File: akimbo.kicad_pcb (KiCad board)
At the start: 2 copper layers, 163.9 x 125.9 mm, 73 parts, among them J1 USB mini-B, J2 3.5mm TRRS, J3 3.5mm TRRS, K1 -, K11 -, K12 -, K13 -, K14 -, K15 -, K16 -, K17 -, K18 -, K19 -, K2 -, K20 -, K21 -, K22 -, K23 -, K24 -, K25 -, K26 -, K27 -, K28 -, K29 -, K3 -, K30 -, K4 -, K6 -, K7 -, K8 -, K9 -, U1 ATmega32U4, U2 MCP23017_SO, Y1 16M

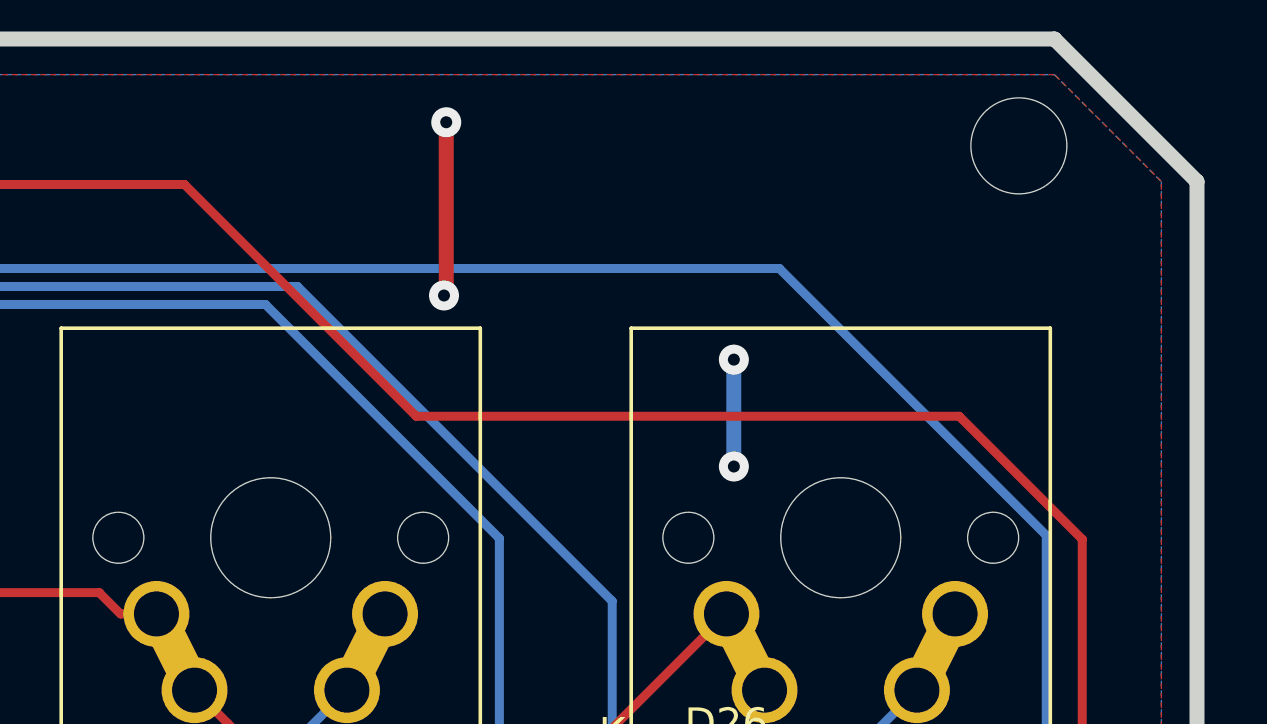
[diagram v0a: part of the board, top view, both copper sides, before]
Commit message: I2C pullups
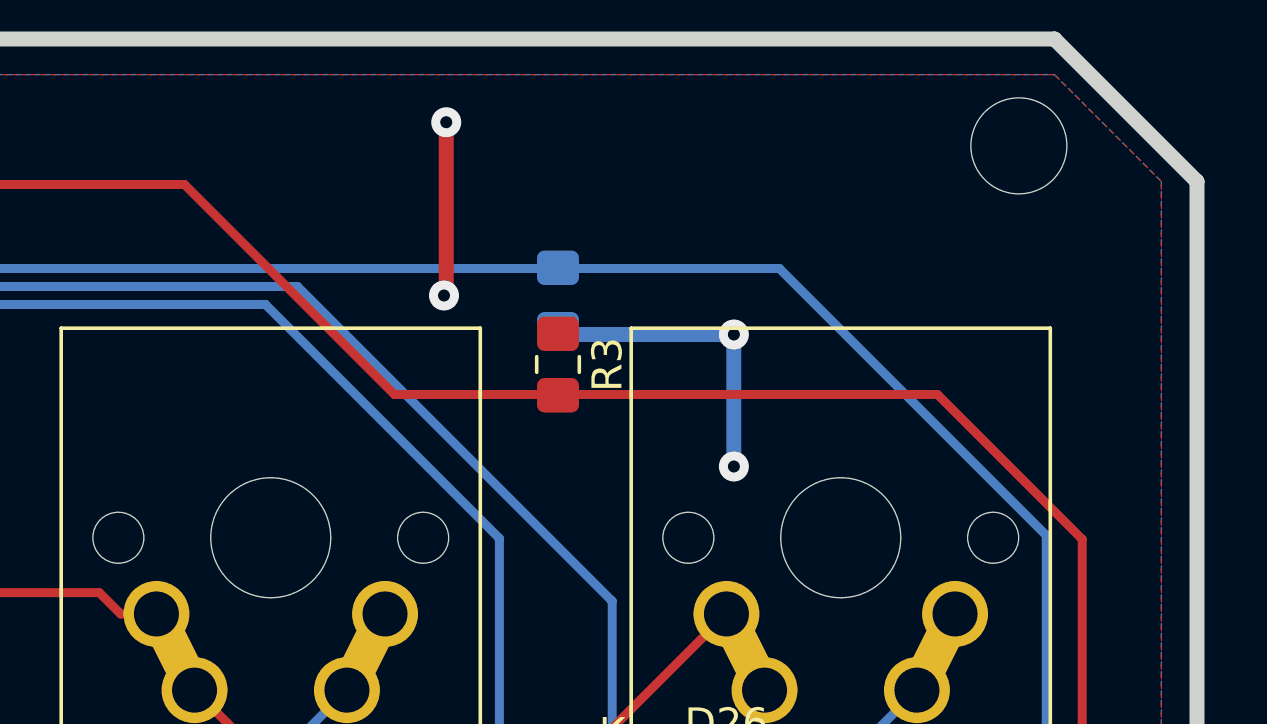
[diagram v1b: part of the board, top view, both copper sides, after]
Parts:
- added R3: 4k7, Resistor_SMD:R_0805_2012Metric_Pad1.15x1.40mm_HandSolder, F.Cu at (121.2, 34.6)
- added R4: 4k7, Resistor_SMD:R_0805_2012Metric_Pad1.15x1.40mm_HandSolder, B.Cu at (121.2, 32.4)
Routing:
- net +5V: track 66.8 -> 73.6 mm
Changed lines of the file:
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@@
     (thickness 1.6)
     (drawings 17)
-    (tracks 577)
+    (tracks 581)
     (zones 0)
-    (modules 73)
+    (modules 75)
     (nets 51)
   )
@@
     (add_net GND)
   )
+  (module Resistor_SMD:R_0805_2012Metric_Pad1.15x1.40mm_HandSolder (layer B.Cu)
+    (at 121.2 32.4 90)
+    (descr "Resistor SMD 0805 (2012 Metric), square (rectangular) end terminal, IPC_7351 nominal with elongated pad for handsoldering. (Body size source: https://docs.google.com/spreadsheets/d/1BsfQQcO9C6DZCsRaXUlFlo91Tg2WpOkGARC1WS5S8t0/edit?usp=sharing), generated with kicad-footprint-generator")
+    (tags "resistor handsolder")
+    (attr smd)
+    (fp_text reference R4 (at 0 1.65 270) (layer B.SilkS)
+      (effects (font (size 1 1) (thickness 0.15)) (justify mirror))
+    )
+    (fp_text value 4k7 (at 0 -1.65 270) (layer B.Fab)
+      (effects (font (size 1 1) (thickness 0.15)) (justify mirror))
+    )
+    (fp_text user %R (at 0 0 270) (layer B.Fab)
+      (effects (font (size 0.5 0.5) (thickness 0.08)) (justify mirror))
+    )
+    (fp_line (start 1.85 -0.95) (end -1.85 -0.95) (layer B.CrtYd) (width 0.05))
+    (fp_line (start 1.85 0.95) (end 1.85 -0.95) (layer B.CrtYd) (width 0.05))
+    (fp_line (start -1.85 0.95) (end 1.85 0.95) (layer B.CrtYd) (width 0.05))
+    (fp_line (start -1.85 -0.95) (end -1.85 0.95) (layer B.CrtYd) (width 0.05))
+    (fp_line (start -0.261252 -0.71) (end 0.261252 -0.71) (layer B.SilkS) (width 0.12))
+    (fp_line (start -0.261252 0.71) (end 0.261252 0.71) (layer B.SilkS) (width 0.12))
+    (fp_line (start 1 -0.6) (end -1 -0.6) (layer B.Fab) (width 0.1))
+    (fp_line (start 1 0.6) (end 1 -0.6) (layer B.Fab) (width 0.1))
+    (fp_line (start -1 0.6) (end 1 0.6) (layer B.Fab) (width 0.1))
+    (fp_line (start -1 -0.6) (end -1 0.6) (layer B.Fab) (width 0.1))
+    (pad 2 smd roundrect (at 1.025 0 90) (size 1.15 1.4) (layers B.Cu B.Paste B.Mask) (roundrect_rratio 0.217391)
+      (net 47 /sda))
+    (pad 1 smd roundrect (at -1.025 0 90) (size 1.15 1.4) (layers B.Cu B.Paste B.Mask) (roundrect_rratio 0.217391)
+      (net 3 +5V))
+    (model ${KISYS3DMOD}/Resistor_SMD.3dshapes/R_0805_2012Metric.wrl
+      (at (xyz 0 0 0))
+      (scale (xyz 1 1 1))
+      (rotate (xyz 0 0 0))
+    )
+  )
+  (module Resistor_SMD:R_0805_2012Metric_Pad1.15x1.40mm_HandSolder (layer F.Cu)
+    (at 121.2 34.6 270)
+    (descr "Resistor SMD 0805 (2012 Metric), square (rectangular) end terminal, IPC_7351 nominal with elongated pad for handsoldering. (Body size source: https://docs.google.com/spreadsheets/d/1BsfQQcO9C6DZCsRaXUlFlo91Tg2WpOkGARC1WS5S8t0/edit?usp=sharing), generated with kicad-footprint-generator")
+    (tags "resistor handsolder")
+    (attr smd)
+    (fp_text reference R3 (at 0 -1.65 90) (layer F.SilkS)
+      (effects (font (size 1 1) (thickness 0.15)))
+    )
+    (fp_text value 4k7 (at 0 1.65 90) (layer F.Fab)
+      (effects (font (size 1 1) (thickness 0.15)))
+    )
+    (fp_text user %R (at 0 0 90) (layer F.Fab)
+      (effects (font (size 0.5 0.5) (thickness 0.08)))
+    )
+    (fp_line (start 1.85 0.95) (end -1.85 0.95) (layer F.CrtYd) (width 0.05))
+    (fp_line (start 1.85 -0.95) (end 1.85 0.95) (layer F.CrtYd) (width 0.05))
+    (fp_line (start -1.85 -0.95) (end 1.85 -0.95) (layer F.CrtYd) (width 0.05))
+    (fp_line (start -1.85 0.95) (end -1.85 -0.95) (layer F.CrtYd) (width 0.05))
+    (fp_line (start -0.261252 0.71) (end 0.261252 0.71) (layer F.SilkS) (width 0.12))
+    (fp_line (start -0.261252 -0.71) (end 0.261252 -0.71) (layer F.SilkS) (width 0.12))
+    (fp_line (start 1 0.6) (end -1 0.6) (layer F.Fab) (width 0.1))
+    (fp_line (start 1 -0.6) (end 1 0.6) (layer F.Fab) (width 0.1))
+    (fp_line (start -1 -0.6) (end 1 -0.6) (layer F.Fab) (width 0.1))
+    (fp_line (start -1 0.6) (end -1 -0.6) (layer F.Fab) (width 0.1))
+    (pad 2 smd roundrect (at 1.025 0 270) (size 1.15 1.4) (layers F.Cu F.Paste F.Mask) (roundrect_rratio 0.217391)
+      (net 48 /sck))
+    (pad 1 smd roundrect (at -1.025 0 270) (size 1.15 1.4) (layers F.Cu F.Paste F.Mask) (roundrect_rratio 0.217391)
+      (net 3 +5V))
+    (model ${KISYS3DMOD}/Resistor_SMD.3dshapes/R_0805_2012Metric.wrl
+      (at (xyz 0 0 0))
+      (scale (xyz 1 1 1))
+      (rotate (xyz 0 0 0))
+    )
+  )
   (module akimbo:SW_Cherry_MX_1.00u_PCB_Reversible (layer F.Cu)
     (at 149.186846 109.486022 135)
@@
   (segment (start 27.675 97.125) (end 31.275 97.125) (width 0.5) (layer B.Cu) (net 3))
   (via (at 24.275 76.725) (size 1) (drill 0.4) (layers F.Cu B.Cu) (net 3))
-  (via (at 127.0625 34.4375) (size 1) (drill 0.4) (layers F.Cu B.Cu) (net 3))
   (via (at 127.0625 38) (size 1) (drill 0.4) (layers F.Cu B.Cu) (net 3))
-  (segment (start 127.0625 34.4375) (end 127.0625 38) (width 0.5) (layer B.Cu) (net 3))
   (via (at 49.8 43) (size 1) (drill 0.4) (layers F.Cu B.Cu) (net 3))
   (segment (start 51.375 39.625) (end 51.375 41.425) (width 0.5) (layer B.Cu) (net 3))
@@
   (segment (start 24.275 58.525) (end 28.4 58.525) (width 0.5) (layer B.Cu) (net 3))
   (via (at 28.4 58.525) (size 1) (drill 0.4) (layers F.Cu B.Cu) (net 3))
+  (via (at 127.062494 33.6) (size 1) (drill 0.4) (layers F.Cu B.Cu) (net 3))
+  (segment (start 127.0625 33.600006) (end 127.062494 33.6) (width 0.5) (layer B.Cu) (net 3))
+  (segment (start 127.0625 38) (end 127.0625 33.600006) (width 0.5) (layer B.Cu) (net 3))
+  (segment (start 121.225 33.6) (end 121.2 33.575) (width 0.5) (layer F.Cu) (net 3))
+  (segment (start 121.375 33.6) (end 121.2 33.425) (width 0.5) (layer B.Cu) (net 3))
+  (segment (start 127.062494 33.6) (end 121.375 33.6) (width 0.5) (layer B.Cu) (net 3))
   (segment (start 41.97 72.4375) (end 40.87 72.4375) (width 0.3) (layer B.Cu) (net 4) (status 20))
   (segment (start 43.245 71.1625) (end 41.97 72.4375) (width 0.3) (layer B.Cu) (net 4))
@@
   (segment (start 57.875 29.925) (end 57.875 32.325) (width 0.3) (layer B.Cu) (net 48))
   (segment (start 57.075 33.125) (end 56.675 33.525) (width 0.3) (layer F.Cu) (net 48))
-  (segment (start 116.475 36.325) (end 108.75 28.6) (width 0.3) (layer F.Cu) (net 48))
   (segment (start 108.75 28.6) (end 73.2 28.6) (width 0.3) (layer F.Cu) (net 48))
   (segment (start 68.675 33.125) (end 57.075 33.125) (width 0.3) (layer F.Cu) (net 48))
-  (segment (start 73.2 28.6) (end 68.675 33.125) (width 0.3) (layer F.Cu) (net 48))
-  (segment (start 134.572256 36.325) (end 116.475 36.325) (width 0.3) (layer F.Cu) (net 48))
-  (segment (start 138.675 40.427744) (end 134.572256 36.325) (width 0.3) (layer F.Cu) (net 48))
   (segment (start 138.675 83.030886) (end 138.675 40.427744) (width 0.3) (layer F.Cu) (net 48))
   (segment (start 143.722057 88.077943) (end 138.675 83.030886) (width 0.3) (layer F.Cu) (net 48))
+  (segment (start 133.847256 35.6) (end 115.75 35.6) (width 0.3) (layer F.Cu) (net 48))
+  (segment (start 73.2 28.6) (end 68.675 33.125) (width 0.3) (layer F.Cu) (net 48))
+  (segment (start 138.675 40.427744) (end 133.847256 35.6) (width 0.3) (layer F.Cu) (net 48))
+  (segment (start 115.75 35.6) (end 108.75 28.6) (width 0.3) (layer F.Cu) (net 48))
   (segment (start 72.675 27.05) (end 72.6 26.975) (width 0.3) (layer B.Cu) (net 49))
   (segment (start 77.35 27.05) (end 72.675 27.05) (width 0.3) (layer B.Cu) (net 49))
@@
     (connect_pads (clearance 0.25))
     (min_thickness 0.25)
-    (fill yes (arc_segments 32) (thermal_gap 0.25) (thermal_bridge_width 0.5))
+    (fill (arc_segments 32) (thermal_gap 0.25) (thermal_bridge_width 0.5))
     (polygon
       (pts
@@
     (connect_pads (clearance 0.25))
     (min_thickness 0.25)
-    (fill yes (arc_segments 32) (thermal_gap 0.25) (thermal_bridge_width 0.5))
+    (fill (arc_segments 32) (thermal_gap 0.25) (thermal_bridge_width 0.5))
     (polygon
       (pts
@@
     (connect_pads (clearance 0.25))
     (min_thickness 0.25)
-    (fill yes (arc_segments 32) (thermal_gap 0.25) (thermal_bridge_width 0.5))
+    (fill (arc_segments 32) (thermal_gap 0.25) (thermal_bridge_width 0.5))
     (polygon
       (pts

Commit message: Tweaked silkscreen; routing tweaks; cleanup
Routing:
- net +5V: track 73.6 -> 85.6 mm, vias 15 -> 16
- net /row3: track 224.7 -> 222.3 mm
- net /row2: track 202.6 -> 201.1 mm
- net /row1: track 178.3 -> 177.6 mm

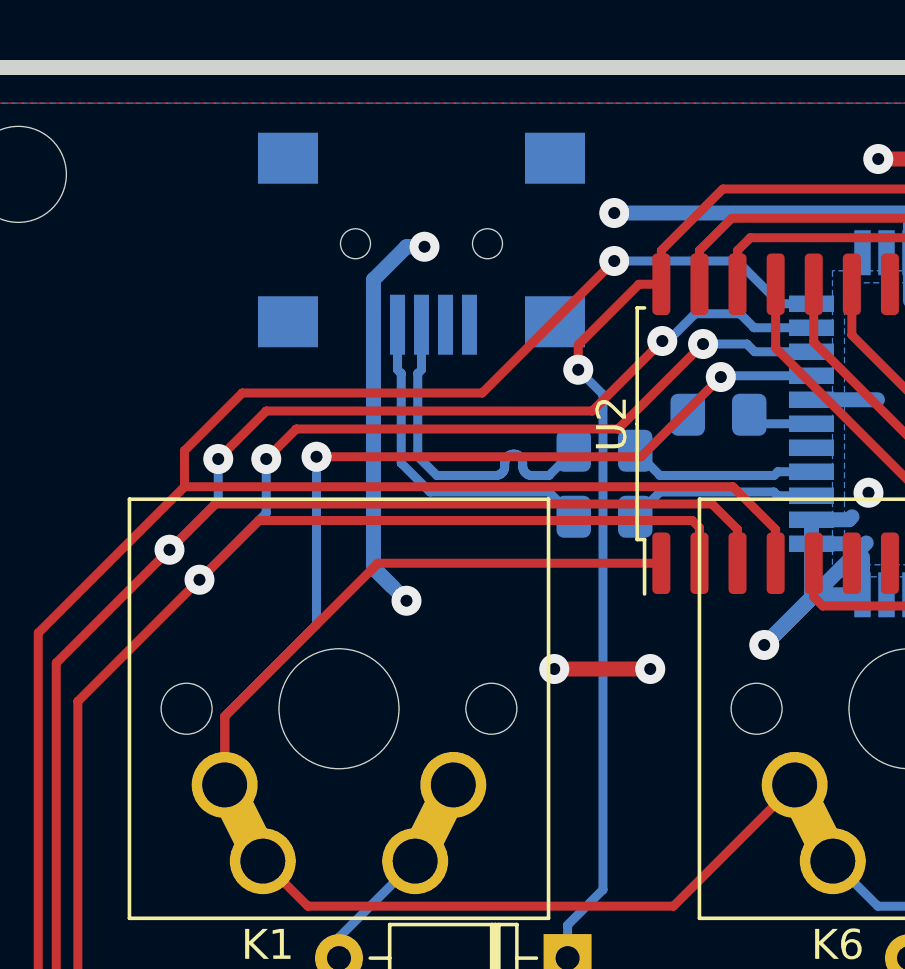
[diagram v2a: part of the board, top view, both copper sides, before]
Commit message: USB-C instead of mini-B
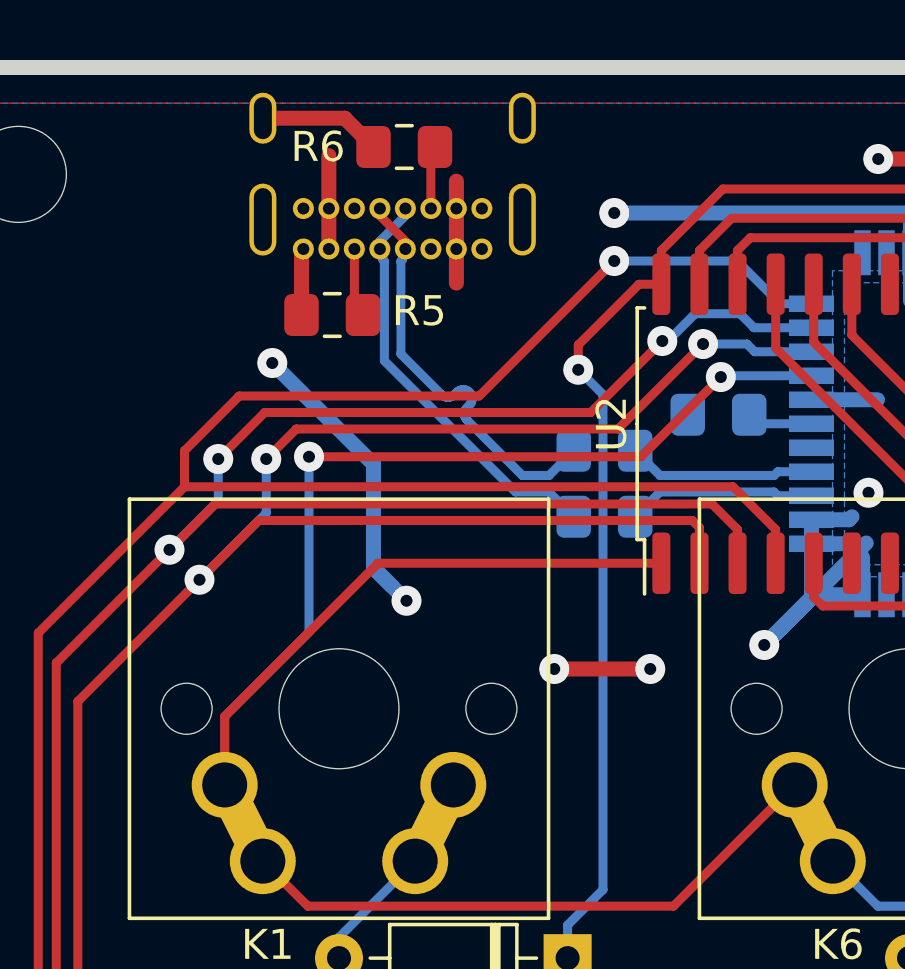
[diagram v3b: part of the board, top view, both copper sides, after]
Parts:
- added R5: 5k1, Resistor_SMD:R_0805_2012Metric_Pad1.15x1.40mm_HandSolder, F.Cu at (35.4, 32.0)
- added R6: 5k1, Resistor_SMD:R_0805_2012Metric_Pad1.15x1.40mm_HandSolder, F.Cu at (37.8, 26.4)
- J1: value USB mini-B -> USB-C; footprint Connector_USB:USB_Mini-B_Lumberg_2486_01_Horizontal -> Connector_USB:USB_C_Receptacle_GCT_USB4085
- moved J1 3.94 mm to (34.4, 29.8)
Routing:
- net GND: track 80.9 -> 87.2 mm
- net +5V: track 85.6 -> 88.6 mm
- net /d+: track 11.2 -> 14.0 mm
- net /d-: track 11.2 -> 14.0 mm
- net Net-(J1-PadA5): track 0.00 -> 2.32 mm
- net Net-(J1-PadB5): track 0.00 -> 2.11 mm
